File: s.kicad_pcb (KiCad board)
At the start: 2 copper layers, 200 x 77.4 mm, 97 parts, among them J2 UART connector, J4 Conn_01x02_Pin, J5 USB4105-GF-A, SW1 Z, SW10 D, SW11 S, SW12 K, SW13 W, SW14 R, SW15 STAR, SW16 R, SW17 B, SW18 G, SW19 S, SW2 T, SW20 Z, SW21 A, SW22 O, SW23 NUM, SW24 E, SW25 U, SW26 210-4MS, SW27 09.03290.01, SW3 P, SW4 H, SW5 STAR, SW6 F, SW7 P, SW8 L, SW9 T, U1 ESP32-S3-WROOM-1, U2 MCP1825S, U3 MCP1825S, U4 AP9101CK, U5 MCP73831-2-OT, U6 DMG6968U-7, U7 DMG6968U-7

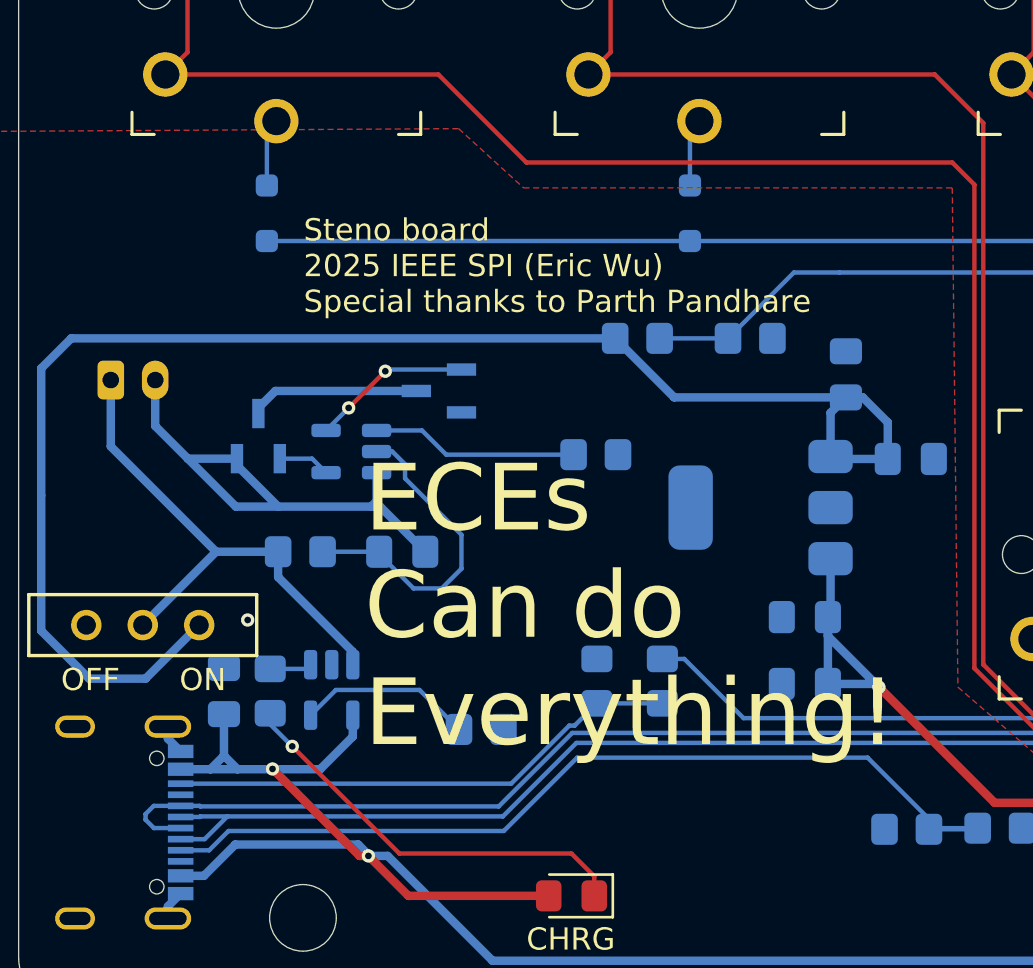
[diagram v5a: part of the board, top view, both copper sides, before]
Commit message: add a few vias
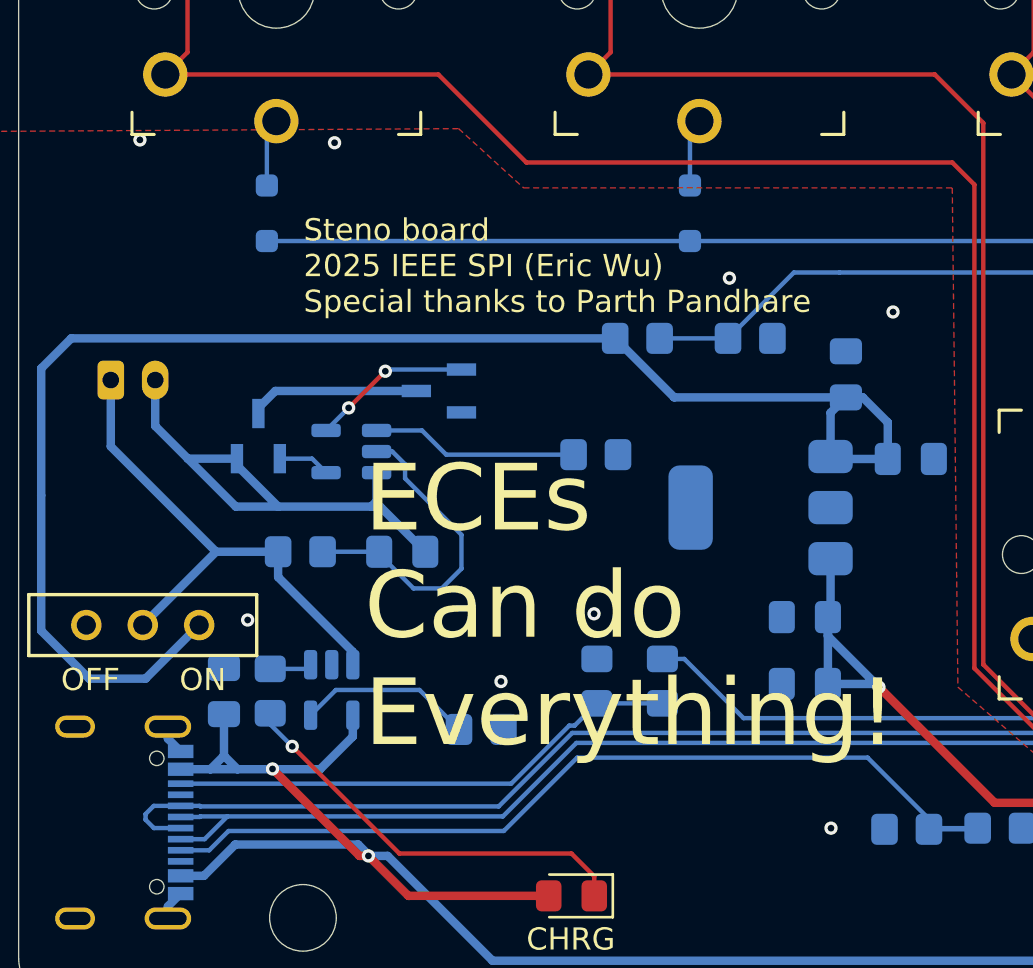
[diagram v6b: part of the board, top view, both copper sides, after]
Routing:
- net GND: vias 12 -> 19
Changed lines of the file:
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@@
+	)
+	(via
+		(at 76.708 121.031)
+		(size 0.6)
+		(drill 0.3)
+		(layers "F.Cu" "B.Cu")
+		(free yes)
+		(net 1)
 	)
 	(via
 		(at 121.793 133.35)
+		(size 0.6)
+		(drill 0.3)
+		(layers "F.Cu" "B.Cu")
+		(free yes)
+		(net 1)
+	)
+	(via
+		(at 82.804 105.918)
 		(size 0.6)
 		(drill 0.3)
@@
 	)
 	(via
+		(at 65.024 99.822)
+		(size 0.6)
+		(drill 0.3)
+		(layers "F.Cu" "B.Cu")
+		(free yes)
+		(net 1)
+	)
+	(via
 		(at 201.7776 134.0612)
+		(size 0.6)
+		(drill 0.3)
+		(layers "F.Cu" "B.Cu")
+		(free yes)
+		(net 1)
+	)
+	(via
+		(at 56.261 99.695)
 		(size 0.6)
 		(drill 0.3)
@@
 	)
 	(via
+		(at 87.376 130.683)
+		(size 0.6)
+		(drill 0.3)
+		(layers "F.Cu" "B.Cu")
+		(free yes)
+		(net 1)
+	)
+	(via
+		(at 72.517 124.079)
+		(size 0.6)
+		(drill 0.3)
+		(layers "F.Cu" "B.Cu")
+		(free yes)
+		(net 1)
+	)
+	(via
 		(at 139.827 133.35)
 		(size 0.6)
 		(drill 0.3)
+		(layers "F.Cu" "B.Cu")
+		(free yes)
+		(net 1)
+	)
+	(via
+		(at 90.17 107.442)
+		(size 0.6)
+		(drill 0.3)

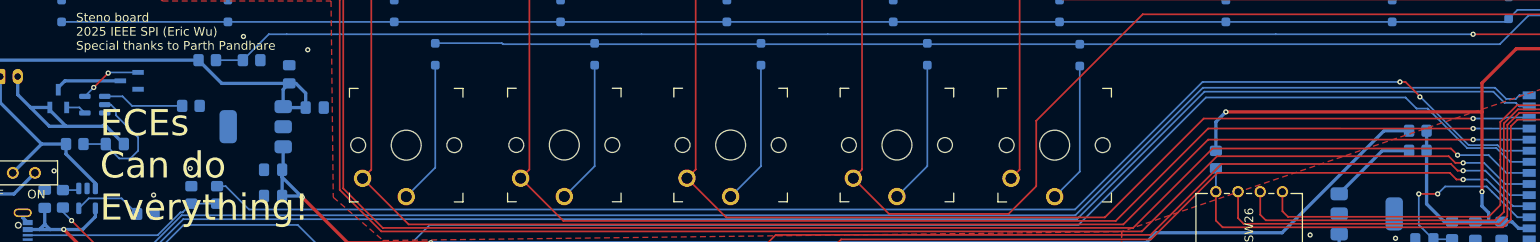
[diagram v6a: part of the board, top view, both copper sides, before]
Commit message: add a push button for RST
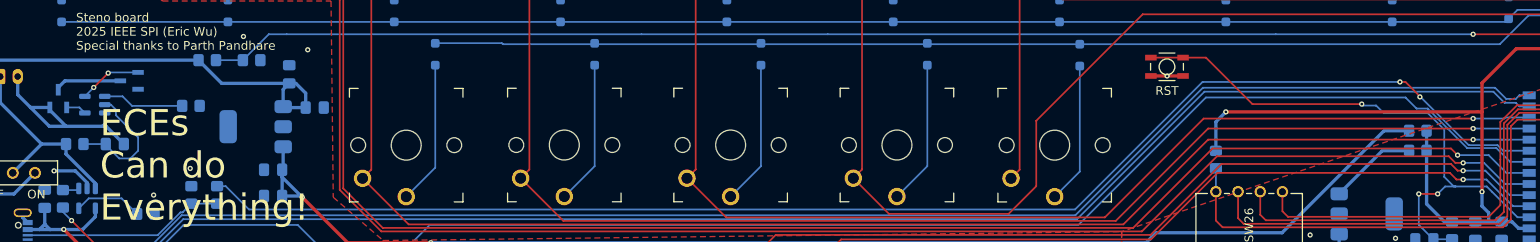
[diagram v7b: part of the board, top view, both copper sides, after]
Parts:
- added RST: EVP-AA202K, push_btn_aa202k:SW_EVP-AA102K_PAN, F.Cu at (188.6, 109.4)
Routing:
- net Net-(U1-EN): track 22.5 -> 66.7 mm, vias 2 -> 3
- net GND: track 10.5 -> 19.2 mm, vias 19 -> 20

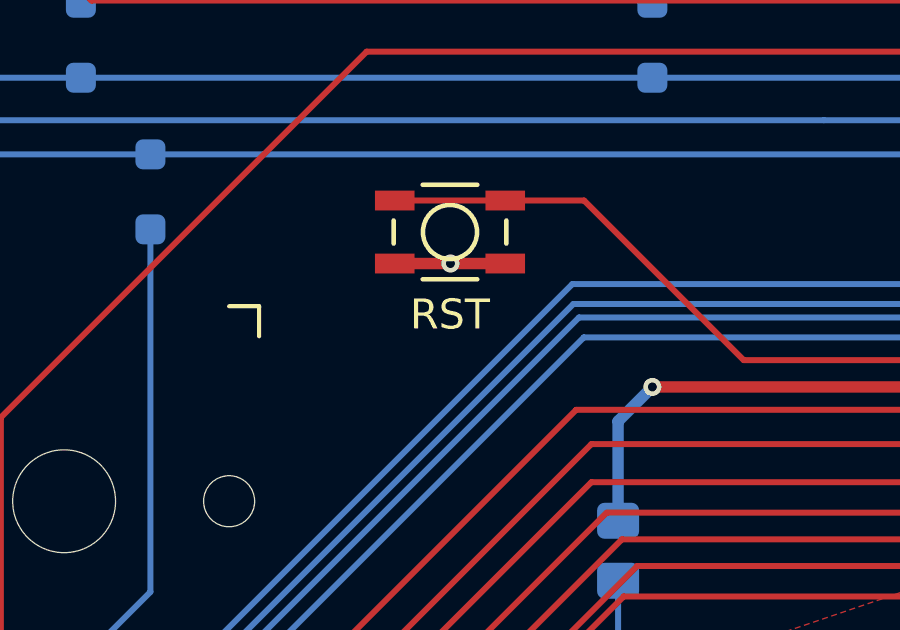
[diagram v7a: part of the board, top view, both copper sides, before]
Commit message: change footprint of JST connector. Vertical -> horizontal
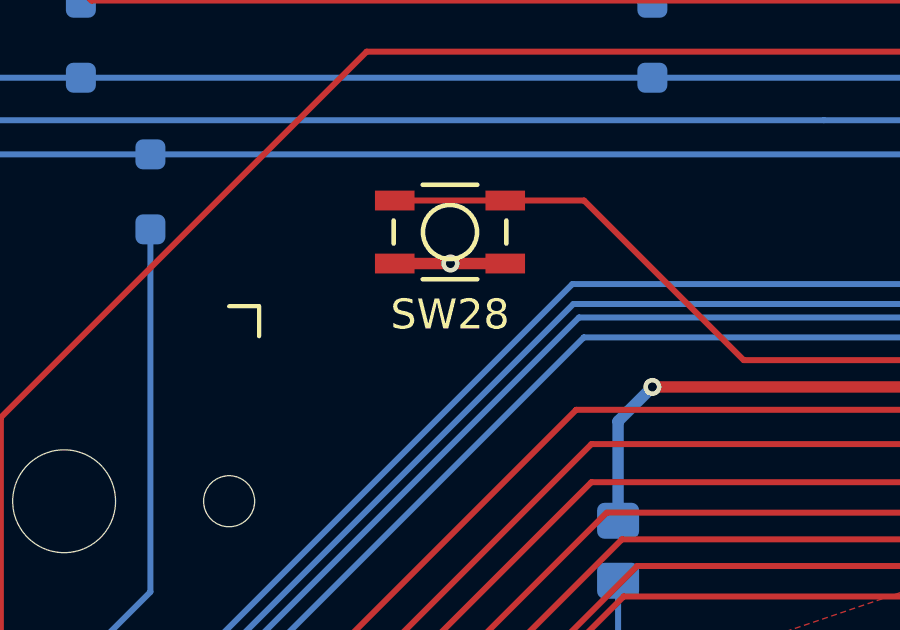
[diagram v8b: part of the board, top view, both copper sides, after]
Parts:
- J4: footprint Connector_JST:JST_PH_B2B-PH-K_1x02_P2.00mm_Vertical -> Connector_JST:JST_PH_S2B-PH-K_1x02_P2.00mm_Horizontal
- renumbered RST to SW28
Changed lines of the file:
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@@
 		(at 188.58 109.39)
 		(tags "EVP-AA202K ")
-		(property "Reference" "RST"
+		(property "Reference" "SW28"
 			(at 0 2.751 0)
 			(unlocked yes)
@@
 		)
 	)
-	(footprint "Connector_JST:JST_PH_B2B-PH-K_1x02_P2.00mm_Vertical"
+	(footprint "Connector_JST:JST_PH_S2B-PH-K_1x02_P2.00mm_Horizontal"
 		(layer "B.Cu")
 		(at 54.949 110.506)
-		(descr "JST PH series connector, B2B-PH-K (http://www.jst-mfg.com/product/pdf/eng/ePH.pdf), generated with kicad-footprint-generator")
-		(tags "connector JST PH vertical")
+		(descr "JST PH series connector, S2B-PH-K (http://www.jst-mfg.com/product/pdf/eng/ePH.pdf), generated with kicad-footprint-generator")
+		(tags "connector JST PH horizontal")
 		(property "Reference" "J4"
-			(at 1 2.9 0)
+			(at 1 2.55 180)
 			(layer "B.SilkS")
 			(effects
@@
 		)
 		(property "Value" "Conn_01x02_Pin"
-			(at 1 -4 0)
+			(at -5.419 -2.683 270)
 			(layer "B.Fab")
 			(effects
@@
 		)
 		(property "Datasheet" "~"
-			(at 0 0 0)
+			(at 0 0 180)
 			(layer "B.Fab")
 			(hide yes)
@@
 		)
 		(property "Description" "Generic connector, single row, 01x02, script generated"
-			(at 0 0 0)
+			(at 0 0 180)
 			(layer "B.Fab")
 			(hide yes)
@@
 		(attr through_hole)
 		(fp_line
-			(start -2.36 2.11)
-			(end -2.36 0.86)
+			(start -2.06 -6.36)
+			(end 4.06 -6.36)
 			(stroke
 				(width 0.12)
@@
 		)
 		(fp_line
-			(start -2.06 -2.91)
-			(end 4.06 -2.91)
+			(start -2.06 -0.14)
+			(end -1.14 -0.14)
 			(stroke
 				(width 0.12)
@@
 		)
 		(fp_line
-			(start -2.06 -0.8)
-			(end -1.45 -0.8)
+			(start -2.06 1.46)
+			(end -2.06 -6.36)
 			(stroke
 				(width 0.12)
@@
 		)
 		(fp_line
-			(start -2.06 0.5)
-			(end -1.45 0.5)
+			(start -1.3 -4.1)
+			(end -0.3 -4.1)
 			(stroke
 				(width 0.12)
@@
 		)
 		(fp_line
-			(start -2.06 1.81)
-			(end -2.06 -2.91)
+			(start -1.3 -2.5)
+			(end -1.3 -4.1)
 			(stroke
 				(width 0.12)
@@
 		)
 		(fp_line
-			(start -1.45 -2.3)
-			(end 3.45 -2.3)
+			(start -1.14 -0.14)
+			(end -1.14 1.46)
 			(stroke
 				(width 0.12)
@@
 		)
 		(fp_line
-			(start -1.45 1.2)
-			(end -1.45 -2.3)
+			(start -1.14 1.46)
+			(end -2.06 1.46)
 			(stroke
 				(width 0.12)
@@
 		)
 		(fp_line
-			(start -1.11 2.11)
-			(end -2.36 2.11)
+			(start -0.86 -0.14)
+			(end -1.14 -0.14)
 			(stroke
 				(width 0.12)
@@
 		)
 		(fp_line
-			(start -0.6 2.01)
-			(end -0.6 1.81)
+			(start -0.86 -0.14)
+			(end -0.86 1.075)
 			(stroke
 				(width 0.12)
@@
 		)
 		(fp_line
-			(start -0.3 1.81)
-			(end -0.3 2.01)
+			(start -0.8 -4.1)
+			(end -0.8 -6.36)
 			(stroke
 				(width 0.12)
@@
 		)
 		(fp_line
-			(start -0.3 1.91)
-			(end -0.6 1.91)
+			(start -0.3 -4.1)
+			(end -0.3 -6.36)
 			(stroke
 				(width 0.12)
@@
 		)
 		(fp_line
-			(start -0.3 2.01)
-			(end -0.6 2.01)
+			(start -0.3 -4.1)
+			(end -0.3 -2.5)
 			(stroke
 				(width 0.12)
@@
 		)
 		(fp_line
-			(start 0.5 1.2)
-			(end -1.45 1.2)
+			(start -0.3 -2.5)
+			(end -1.3 -2.5)
 			(stroke
 				(width 0.12)
@@
 		)
 		(fp_line
-			(start 0.5 1.81)
-			(end 0.5 1.2)
+			(start 0.5 -6.36)
+			(end 0.5 -2)
 			(stroke
 				(width 0.12)
@@
 		)
 		(fp_line
-			(start 0.9 -2.3)
-			(end 0.9 -1.8)
+			(start 0.5 -2)
+			(end 1.5 -2)
 			(stroke
 				(width 0.12)
@@
 		)
 		(fp_line
-			(start 0.9 -1.8)
-			(end 1.1 -1.8)
+			(start 1.5 -2)
+			(end 1.5 -6.36)
 			(stroke
 				(width 0.12)
@@
 		)
 		(fp_line
-			(start 1 -2.3)
-			(end 1 -1.8)
+			(start 2.3 -4.1)
+			(end 2.3 -2.5)
 			(stroke
 				(width 0.12)
@@
 		)
 		(fp_line
-			(start 1.1 -1.8)
-			(end 1.1 -2.3)
+			(start 2.3 -2.5)
+			(end 3.3 -2.5)
 			(stroke
 				(width 0.12)
@@
 		)
 		(fp_line
-			(start 1.5 1.2)
-			(end 1.5 1.81)
+			(start 3.14 -0.14)
+			(end 2.86 -0.14)
 			(stroke
 				(width 0.12)
@@
 		)
 		(fp_line
-			(start 3.45 -2.3)
-			(end 3.45 1.2)
+			(start 3.14 1.46)
+			(end 3.14 -0.14)
 			(stroke
 				(width 0.12)
@@
 		)
 		(fp_line
-			(start 3.45 1.2)
-			(end 1.5 1.2)
+			(start 3.3 -4.1)
+			(end 2.3 -4.1)
 			(stroke
 				(width 0.12)
@@
 		)
 		(fp_line
-			(start 4.06 -2.91)
-			(end 4.06 1.81)
+			(start 3.3 -2.5)
+			(end 3.3 -4.1)
 			(stroke
 				(width 0.12)
@@
 		)
 		(fp_line
-			(start 4.06 -0.8)
-			(end 3.45 -0.8)
+			(start 4.06 -6.36)
+			(end 4.06 1.46)
 			(stroke
 				(width 0.12)
@@
 		)
 		(fp_line
-			(start 4.06 0.5)
-			(end 3.45 0.5)
+			(start 4.06 -0.14)
+			(end 3.14 -0.14)
 			(stroke
 				(width 0.12)
@@
 		)
 		(fp_line
-			(start 4.06 1.81)
-			(end -2.06 1.81)
+			(start 4.06 1.46)
+			(end 3.14 1.46)
 			(stroke
 				(width 0.12)
@@
 		)
 		(fp_line
-			(start -2.45 -3.3)
-			(end 4.45 -3.3)
+			(start -2.45 -6.75)
+			(end 4.45 -6.75)
 			(stroke
 				(width 0.05)
@@
 		)
 		(fp_line
-			(start -2.45 2.2)
-			(end -2.45 -3.3)
+			(start -2.45 1.85)
+			(end -2.45 -6.75)
 			(stroke
 				(width 0.05)
@@
 		)
 		(fp_line
-			(start 4.45 -3.3)
-			(end 4.45 2.2)
+			(start 4.45 -6.75)
+			(end 4.45 1.85)
 			(stroke
 				(width 0.05)
@@
 		)
 		(fp_line
-			(start 4.45 2.2)
-			(end -2.45 2.2)
+			(start 4.45 1.85)
+			(end -2.45 1.85)
 			(stroke
 				(width 0.05)
@@
 		)
 		(fp_line
-			(start -2.36 2.11)
-			(end -2.36 0.86)
+			(start -1.95 -6.25)
+			(end 3.95 -6.25)
+			(stroke
+				(width 0.1)
+				(type solid)
+			)
+			(layer "B.Fab")
+		)
+		(fp_line
+			(start -1.95 1.35)
+			(end -1.95 -6.25)
+			(stroke
+				(width 0.1)
+				(type solid)
+			)
+			(layer "B.Fab")
+		)
+		(fp_line
+			(start -1.25 -0.25)
+			(end -1.25 1.35)
+			(stroke
+				(width 0.1)
+				(type solid)
+			)
+			(layer "B.Fab")
+		)
+		(fp_line
+			(start -1.25 1.35)
+			(end -1.95 1.35)
+			(stroke
+				(width 0.1)
+				(type solid)
+			)
+			(layer "B.Fab")
+		)
+		(fp_line
+			(start -0.5 -1.375)
+			(end 0.5 -1.375)
+			(stroke
+				(width 0.1)
+				(type solid)
+			)
+			(layer "B.Fab")
+		)
+		(fp_line
+			(start 0 -0.875)
+			(end -0.5 -1.375)
 			(stroke
 				(width 0.1)
@@
 		)
 		(fp_line
-			(start -1.95 -2.8)
-			(end 3.95 -2.8)
+			(start 0.5 -1.375)
+			(end 0 -0.875)
 			(stroke
 				(width 0.1)
@@
 		)
 		(fp_line
-			(start -1.95 1.7)
-			(end -1.95 -2.8)
+			(start 3.25 -0.25)
+			(end -1.25 -0.25)
 			(stroke
 				(width 0.1)
@@
 		)
 		(fp_line
-			(start -1.11 2.11)
-			(end -2.36 2.11)
+			(start 3.25 1.35)
+			(end 3.25 -0.25)
 			(stroke
 				(width 0.1)
@@
 		)
 		(fp_line
-			(start 3.95 -2.8)
-			(end 3.95 1.7)
+			(start 3.95 -6.25)
+			(end 3.95 1.35)
 			(stroke
 				(width 0.1)
@@
 		)
 		(fp_line
-			(start 3.95 1.7)
-			(end -1.95 1.7)
+			(start 3.95 1.35)
+			(end 3.25 1.35)
 			(stroke
 				(width 0.1)
@@
 		)
 		(fp_text user "${REFERENCE}"
-			(at 1 -1.5 0)
+			(at 1 -2.5 180)
 			(layer "B.Fab")
 			(effects
@@
 		)
 		(embedded_fonts no)
-		(model "${KICAD9_3DMODEL_DIR}/Connector_JST.3dshapes/JST_PH_B2B-PH-K_1x02_P2.00mm_Vertical.step"
+		(model "${KICAD9_3DMODEL_DIR}/Connector_JST.3dshapes/JST_PH_S2B-PH-K_1x02_P2.00mm_Horizontal.step"
 			(offset
 				(xyz 0 0 0)
